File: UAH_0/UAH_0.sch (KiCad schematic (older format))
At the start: 64 parts, among them X17 Check_point, X18 Check_point, X2 Check_point, X3 Крепежное_отверстие_М3, X4 Крепежное_отверстие_М3, X5 Крепежное_отверстие_М3, X6 Крепежное_отверстие_М3, X7 LOGO_NIKITOS_19х7

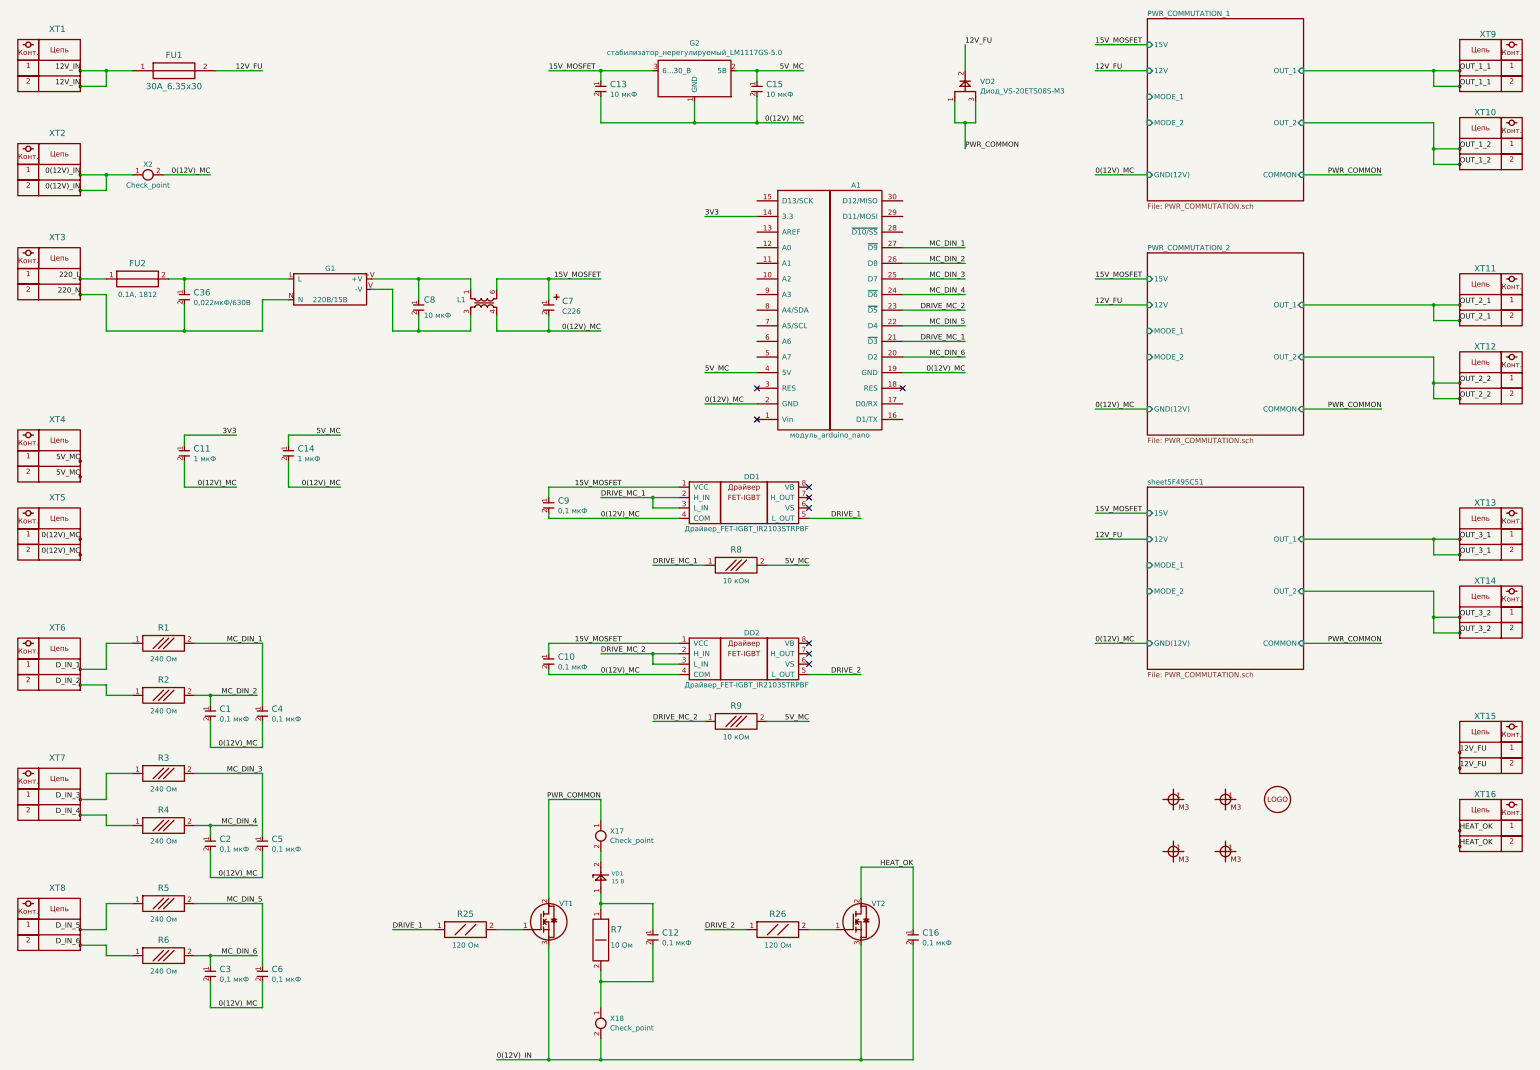
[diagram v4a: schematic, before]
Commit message: закончена трассировка, надо добавить лого и маркировка, PDF обновлен
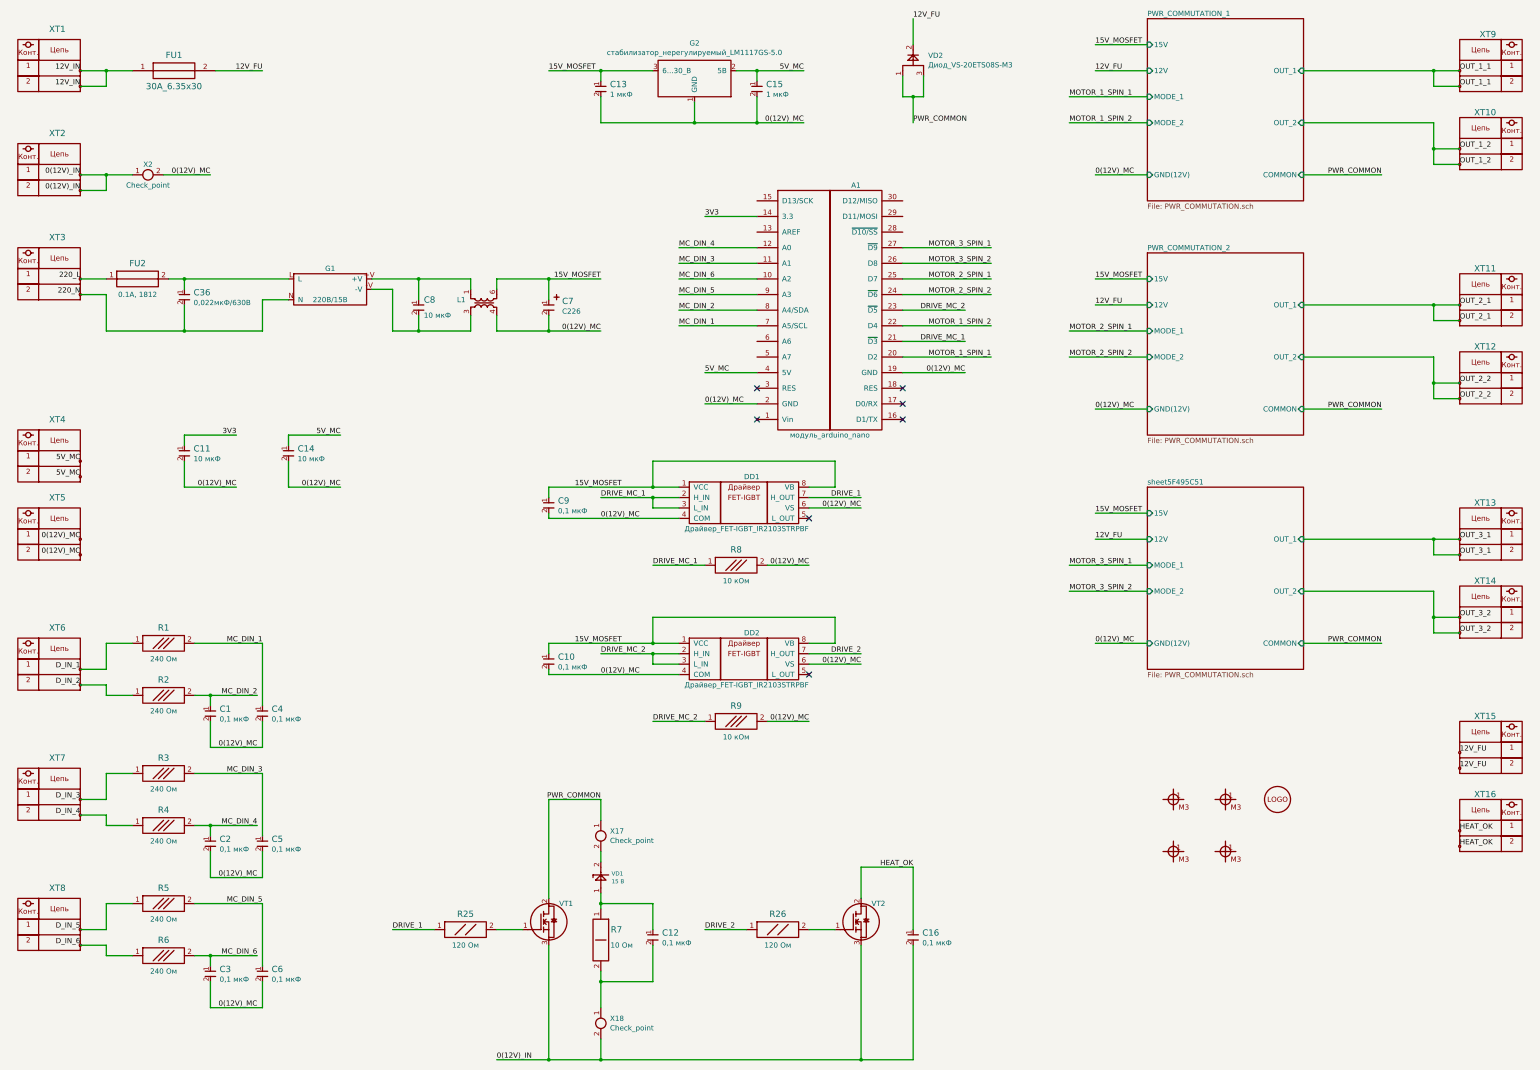
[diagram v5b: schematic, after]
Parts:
- C11, C14: INFO 1 мкФ -> 10 мкФ
- C13, C15: footprint MOTOR_RLC:Конденсатор_SMD_0805 -> MOTOR_RLC:Конденсатор_SMD_К10-83(0603); INFO 10 мкФ -> 1 мкФ
- C8: footprint MOTOR_RLC:Конденсатор_SMD_0805 -> MOTOR_RLC:Конденсатор_SMD_К10-83(0603)
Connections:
- net 0(12V)_MC: now also DD1.6 (VS), DD2.6 (VS), R8.2, R9.2
- net 15V_MOSFET: now also DD1.8 (VB), DD2.8 (VB)
- net 5V_MC: no longer R8.2, R9.2
- net DRIVE_1: now also DD1.7 (H_OUT); no longer DD1.5 (L_OUT)
- net DRIVE_2: now also DD2.7 (H_OUT); no longer DD2.5 (L_OUT)
- net MC_DIN_1: now also A1.7 (A5/SCL); no longer A1.27 (~D9)
- net MC_DIN_2: now also A1.8 (A4/SDA); no longer A1.26 (D8)
- net MC_DIN_3: now also A1.11 (A1); no longer A1.25 (D7)
- net MC_DIN_4: now also A1.12 (A0); no longer A1.24 (~D6)
- net MC_DIN_5: now also A1.9 (A3); no longer A1.22 (D4)
- net MC_DIN_6: now also A1.10 (A2); no longer A1.20 (D2)
- new net MOTOR_1_SPIN_1: A1.20 (D2)
- new net MOTOR_1_SPIN_2: A1.22 (D4)
- new net MOTOR_2_SPIN_1: A1.25 (D7)
- new net MOTOR_2_SPIN_2: A1.24 (~D6)
- new net MOTOR_3_SPIN_1: A1.27 (~D9)
- new net MOTOR_3_SPIN_2: A1.26 (D8)
- no-connect marks 9 -> 7
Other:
- moved on the sheet: VD2
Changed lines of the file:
@@
 F 0 "C15" V 7980 1738 60  0000 L CNN
 F 1 "Конденсатор_16В_10_мкФ+-10проц." H 7950 1400 60  0001 C CNN
-F 2 "MOTOR_RLC:Конденсатор_SMD_0805" H 7900 1500 60  0001 C CNN
+F 2 "MOTOR_RLC:Конденсатор_SMD_К10-83(0603)" H 7900 1500 60  0001 C CNN
 F 3 "${MOTOR_2020_LIB}\\documentation\\IMPORT\\murata_smd_ceramic_cap.pdf" H 8000 1650 60  0001 C CNN
-F 4 "10 мкФ" V 8078 1738 50  0000 L CNN "INFO"
+F 4 "1 мкФ" V 8078 1738 50  0000 L CNN "INFO"
 F 5 "https://www.chipdip.ru/product/grm21br61c106ke15l" H 7875 1900 50  0001 C CNN "LINK"
 	1    8000 1650
@@
 F 0 "C8" V 4700 3800 60  0000 L CNN
 F 1 "Конденсатор_16В_10_мкФ+-10проц." H 4700 3500 60  0001 C CNN
-F 2 "MOTOR_RLC:Конденсатор_SMD_0805" H 4650 3600 60  0001 C CNN
+F 2 "MOTOR_RLC:Конденсатор_SMD_К10-83(0603)" H 4650 3600 60  0001 C CNN
 F 3 "${MOTOR_2020_LIB}\\documentation\\IMPORT\\murata_smd_ceramic_cap.pdf" H 4750 3750 60  0001 C CNN
 F 4 "10 мкФ" V 4850 3800 50  0000 L CNN "INFO"
@@
 L elements_2020:Диод_VS-20ETS08S-M3 VD?
 U 1 1 5F3B01BC
-P 9900 1800
+P 9400 1550
 AR Path="/5F33B5F7/5F3B01BC" Ref="VD?"  Part="1"
 AR Path="/5F48FE9A/5F3B01BC" Ref="VD?"  Part="1"
 AR Path="/5F495C51/5F3B01BC" Ref="VD?"  Part="1"
 AR Path="/5F3B01BC" Ref="VD2"  Part="1"
-F 0 "VD2" H 10144 1996 50  0000 L CNN
-F 1 "Диод_VS-20ETS08S-M3" H 10144 1905 50  0000 L CNN
-F 2 "N_VD_HL:Транзистор_N-канал_dpak" H 10225 1600 50  0001 C CNN
-F 3 "" V 9900 1700 50  0001 C CNN
-	1    9900 1800
-	1    0    0    -1
-$EndComp
-Text Label 10000 2250 0    50   ~ 0
+F 0 "VD2" H 9644 1746 50  0000 L CNN
+F 1 "Диод_VS-20ETS08S-M3" H 9644 1655 50  0000 L CNN
+F 2 "N_VD_HL:Транзистор_N-канал_dpak" H 9725 1350 50  0001 C CNN
+F 3 "" V 9400 1450 50  0001 C CNN
+	1    9400 1550
+	1    0    0    -1
+$EndComp
+Text Label 9500 2000 0    50   ~ 0
 PWR_COMMON
-Text Label 10000 1250 0    50   ~ 0
+Text Label 9500 1000 0    50   ~ 0
 12V_FU
 Wire Wire Line
-	10000 1250 10000 1500
-Wire Wire Line
-	9900 1800 9900 2000
-Wire Wire Line
-	9900 2000 10000 2000
-Wire Wire Line
-	10100 2000 10100 1800
-Wire Wire Line
-	10000 2000 10000 2250
-Connection ~ 10000 2000
-Wire Wire Line
-	10000 2000 10100 2000
+	9500 1000 9500 1250
+Wire Wire Line
+	9400 1550 9400 1750
+Wire Wire Line
+	9400 1750 9500 1750
+Wire Wire Line
+	9600 1750 9600 1550
+Wire Wire Line
+	9500 1750 9500 2000
+Connection ~ 9500 1750
+Wire Wire Line
+	9500 1750 9600 1750
 $Comp
 L elements_2020:Check_point X?
@@
 Wire Wire Line
 	8500 6250 8100 6250
-Text Label 8500 6250 2    50   ~ 0
-5V_MC
 Wire Wire Line
 	7000 6250 7500 6250
@@
 	6000 5800 7250 5800
 Wire Wire Line
-	6000 5500 7250 5500
+	6000 5500 7000 5500
 Text Label 6500 5600 0    50   ~ 0
 DRIVE_MC_1
@@
 	6000 5500 6000 5600
 Wire Wire Line
-	8500 5800 9000 5800
-Text Label 9000 5800 2    50   ~ 0
+	8500 5600 9000 5600
+Text Label 9000 5600 2    50   ~ 0
 DRIVE_1
 Text Label 6500 5800 0    50   ~ 0
@@
 Text Label 6250 5500 0    50   ~ 0
 15V_MOSFET
-NoConn ~ 8500 5500
-NoConn ~ 8500 5700
-NoConn ~ 8500 5600
 $Comp
 L MOTOR_2020_import:Конденсатор_16В_0.1_мкФ+-10проц. C?
@@
 F 2 "MOTOR_RLC:Конденсатор_SMD_К10-83(0603)" H 3400 5000 60  0001 C CNN
 F 3 "${MOTOR_2020_LIB}\\documentation\\IMPORT\\murata_smd_ceramic_cap.pdf" H 3500 5150 60  0001 C CNN
-F 4 "1 мкФ" V 3578 5238 50  0000 L CNN "INFO"
+F 4 "10 мкФ" V 3578 5238 50  0000 L CNN "INFO"
 F 5 "https://www.chipdip.ru/product/grm21br61c106ke15l" H 3375 5400 50  0001 C CNN "LINK"
 	1    3500 5150
@@
 F 2 "MOTOR_RLC:Конденсатор_SMD_К10-83(0603)" H 2400 5000 60  0001 C CNN
 F 3 "${MOTOR_2020_LIB}\\documentation\\IMPORT\\murata_smd_ceramic_cap.pdf" H 2500 5150 60  0001 C CNN
-F 4 "1 мкФ" V 2578 5238 50  0000 L CNN "INFO"
+F 4 "10 мкФ" V 2578 5238 50  0000 L CNN "INFO"
 F 5 "https://www.chipdip.ru/product0/9000591947" H 2375 5400 50  0001 C CNN "LINK"
 	1    2500 5150
@@
 Wire Wire Line
 	8500 7750 8100 7750
-Text Label 8500 7750 2    50   ~ 0
-5V_MC
 Wire Wire Line
 	7000 7750 7500 7750
@@
 	6000 7300 7250 7300
 Wire Wire Line
-	6000 7000 7250 7000
+	6000 7000 7000 7000
 Text Label 6500 7100 0    50   ~ 0
 DRIVE_MC_2
@@
 	6000 7000 6000 7100
 Wire Wire Line
-	8500 7300 9000 7300
-Text Label 9000 7300 2    50   ~ 0
+	8500 7100 9000 7100
+Text Label 9000 7100 2    50   ~ 0
 DRIVE_2
 Text Label 6500 7300 0    50   ~ 0
@@
 Text Label 6250 7000 0    50   ~ 0
 15V_MOSFET
-NoConn ~ 8500 7000
-NoConn ~ 8500 7200
-NoConn ~ 8500 7100
 $Comp
 L MOTOR_2020_import:Конденсатор_16В_0.1_мкФ+-10проц. C?
@@
 Wire Wire Line
 	7250 7200 7000 7200
-$Comp
-L elements_2020:Драйвер_FET-IGBT_IR2103STRPBF DD2
-U 1 1 5F6D5F79
-P 7250 7000
-AR Path="/5F6D5F79" Ref="DD2"  Part="1"
-AR Path="/5F33B5F7/5F6D5F79" Ref="DD?"  Part="1"
-F 0 "DD2" H 7950 7100 50  0000 C CNN
-F 1 "Драйвер_FET-IGBT_IR2103STRPBF" H 7900 6600 50  0000 C CNN
-F 2 "N_DD:SO-8" H 7250 7000 50  0001 C CNN
-F 3 "" H 7250 7000 50  0001 C CNN
-	1    7250 7000
-	1    0    0    -1
-$EndComp
 Wire Wire Line
 	7000 9900 7000 10250
@@
 F 0 "C13" V 6480 1738 60  0000 L CNN
 F 1 "Конденсатор_16В_10_мкФ+-10проц." H 6450 1400 60  0001 C CNN
-F 2 "MOTOR_RLC:Конденсатор_SMD_0805" H 6400 1500 60  0001 C CNN
+F 2 "MOTOR_RLC:Конденсатор_SMD_К10-83(0603)" H 6400 1500 60  0001 C CNN
 F 3 "${MOTOR_2020_LIB}\\documentation\\IMPORT\\murata_smd_ceramic_cap.pdf" H 6500 1650 60  0001 C CNN
-F 4 "10 мкФ" V 6578 1738 50  0000 L CNN "INFO"
+F 4 "1 мкФ" V 6578 1738 50  0000 L CNN "INFO"
 F 5 "https://www.chipdip.ru/product/grm21br61c106ke15l" H 6375 1900 50  0001 C CNN "LINK"
 	1    6500 1650
@@
 	6500 11000 9000 11000
 Connection ~ 6500 11000
+Text Label 10000 4100 2    50   ~ 0
+DRIVE_MC_1
+Wire Wire Line
+	9400 4100 10000 4100
+Text Label 7250 3950 0    50   ~ 0
+MC_DIN_1
+Text Label 7250 3800 0    50   ~ 0
+MC_DIN_2
+Text Label 7250 3200 0    50   ~ 0
+MC_DIN_4
+Wire Wire Line
+	7250 3200 8000 3200
+Wire Wire Line
+	7250 3350 8000 3350
+Wire Wire Line
+	7250 3950 8000 3950
+Text Label 11000 1750 0    50   ~ 0
+MOTOR_1_SPIN_1
+Wire Wire Line
+	11750 1750 11000 1750
+Text Label 11000 2000 0    50   ~ 0
+MOTOR_1_SPIN_2
+Wire Wire Line
+	11750 2000 11000 2000
+Text Label 11000 4000 0    50   ~ 0
+MOTOR_2_SPIN_1
+Wire Wire Line
+	11750 4000 11000 4000
+Text Label 11000 4250 0    50   ~ 0
+MOTOR_2_SPIN_2
+Wire Wire Line
+	11750 4250 11000 4250
+Text Label 11000 6250 0    50   ~ 0
+MOTOR_3_SPIN_1
+Wire Wire Line
+	11750 6250 11000 6250
+Text Label 11000 6500 0    50   ~ 0
+MOTOR_3_SPIN_2
+Wire Wire Line
+	11750 6500 11000 6500
+NoConn ~ 9400 4700
+NoConn ~ 9400 4850
+Wire Wire Line
+	7250 3650 8000 3650
+Wire Wire Line
+	7250 3500 8000 3500
+Text Label 7250 3500 0    50   ~ 0
+MC_DIN_6
+Text Label 7250 3650 0    50   ~ 0
+MC_DIN_5
+Wire Wire Line
+	7250 3800 8000 3800
+Text Label 7250 3350 0    50   ~ 0
+MC_DIN_3
+Wire Wire Line
+	10000 3800 9400 3800
 Text Label 10000 3800 2    50   ~ 0
 DRIVE_MC_2
-Text Label 10000 4100 2    50   ~ 0
-DRIVE_MC_1
-Wire Wire Line
-	10000 3800 9400 3800
-Wire Wire Line
-	9400 4100 10000 4100
-Text Label 10000 3200 2    50   ~ 0
-MC_DIN_1
-Text Label 10000 3350 2    50   ~ 0
-MC_DIN_2
-Text Label 10000 3500 2    50   ~ 0
-MC_DIN_3
-Text Label 10000 3650 2    50   ~ 0
-MC_DIN_4
-Text Label 10000 3950 2    50   ~ 0
-MC_DIN_5
-Text Label 10000 4250 2    50   ~ 0
-MC_DIN_6
-Wire Wire Line
-	10000 3200 9400 3200
-Wire Wire Line
-	10000 3350 9400 3350
-Wire Wire Line
-	10000 3500 9400 3500
-Wire Wire Line
-	10000 3650 9400 3650
-Wire Wire Line
-	10000 3950 9400 3950
-Wire Wire Line
-	10000 4250 9400 4250
+Text Label 10250 4250 2    50   ~ 0
+MOTOR_1_SPIN_1
+Text Label 10250 3950 2    50   ~ 0
+MOTOR_1_SPIN_2
+Text Label 10250 3500 2    50   ~ 0
+MOTOR_2_SPIN_1
+Text Label 10250 3650 2    50   ~ 0
+MOTOR_2_SPIN_2
+Text Label 10250 3200 2    50   ~ 0
+MOTOR_3_SPIN_1
+Wire Wire Line
+	10250 4250 9400 4250
+Wire Wire Line
+	10250 3950 9400 3950
+Wire Wire Line
+	10250 3650 9400 3650
+Wire Wire Line
+	10250 3500 9400 3500
+Wire Wire Line
+	10250 3350 9400 3350
+Wire Wire Line
+	10250 3200 9400 3200
+Text Label 10250 3350 2    50   ~ 0
+MOTOR_3_SPIN_2
+$Comp
+L elements_2020:Драйвер_FET-IGBT_IR2103STRPBF DD2
+U 1 1 5F6D5F79
+P 7250 7000
+AR Path="/5F6D5F79" Ref="DD2"  Part="1"
+AR Path="/5F33B5F7/5F6D5F79" Ref="DD?"  Part="1"
+F 0 "DD2" H 7950 7100 50  0000 C CNN
+F 1 "Драйвер_FET-IGBT_IR2103STRPBF" H 7900 6600 50  0000 C CNN
+F 2 "N_DD:SO-8" H 7250 7000 50  0001 C CNN
+F 3 "" H 7250 7000 50  0001 C CNN
+	1    7250 7000
+	1    0    0    -1
+$EndComp
+Text Label 8500 7750 2    50   ~ 0
+0(12V)_MC
+Text Label 8500 6250 2    50   ~ 0
+0(12V)_MC
+Wire Wire Line
+	8750 5500 8500 5500
+Connection ~ 7000 5500
+Wire Wire Line
+	7000 5500 7250 5500
+Wire Wire Line
+	7000 7000 7000 6750
+Wire Wire Line
+	7000 6750 8750 6750
+Wire Wire Line
+	8750 6750 8750 7000
+Wire Wire Line
+	8750 7000 8500 7000
+Connection ~ 7000 7000
+Wire Wire Line
+	7000 7000 7250 7000
+Wire Wire Line
+	7000 5250 8750 5250
+Wire Wire Line
+	7000 5250 7000 5500
+Wire Wire Line
+	8750 5250 8750 5500
+Text Label 9000 5700 2    50   ~ 0
+0(12V)_MC
+Text Label 9000 7200 2    50   ~ 0
+0(12V)_MC
+Wire Wire Line
+	9000 7200 8500 7200
+Wire Wire Line
+	9000 5700 8500 5700
+NoConn ~ 8500 5800
+NoConn ~ 8500 7300
 $EndSCHEMATC
